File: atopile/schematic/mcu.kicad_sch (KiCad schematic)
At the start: 32 parts, among them J1 Tag-Connect_TC2030-IDC-NL_2x0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, SW1 SKRPACE010, SW2 SKRPACE010, U4 ABM8-272-T3, U5 RP2354A

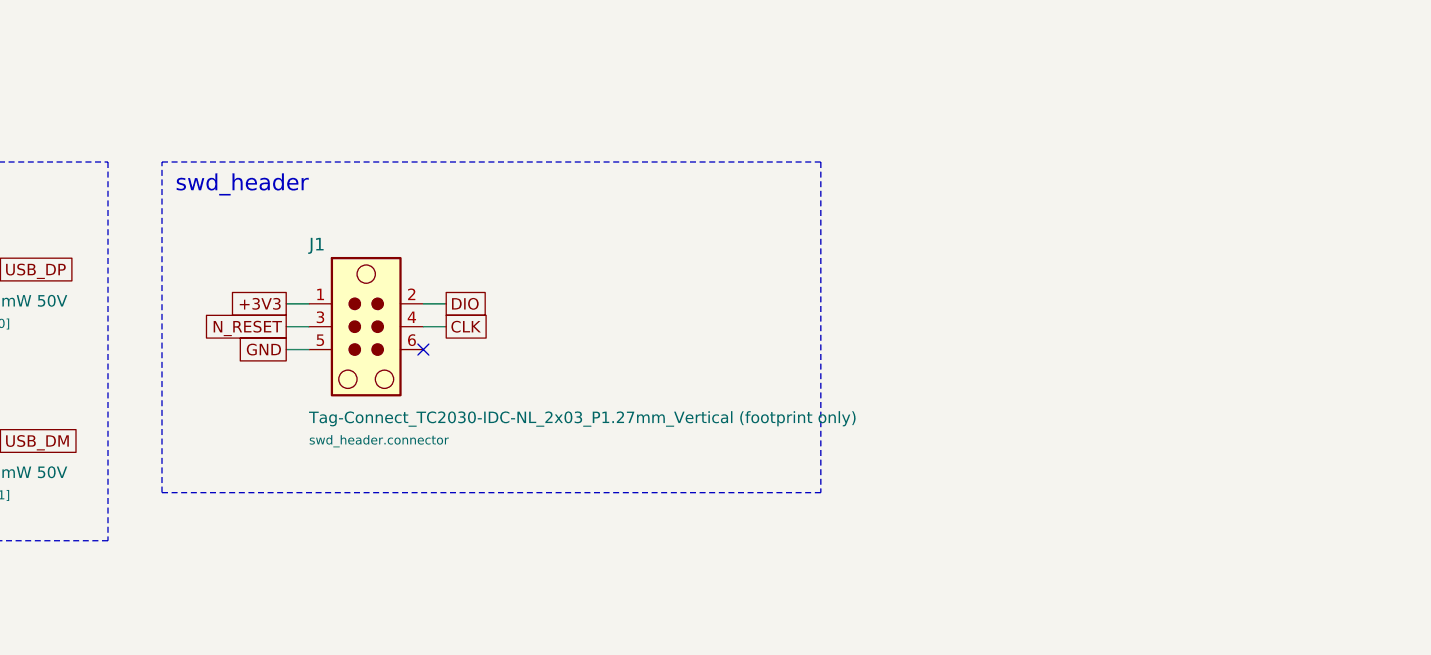
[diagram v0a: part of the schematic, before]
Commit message: Run ERC on the schematic; confirm Hi-Z command inputs are inactive
Schematic export:
- Assign real electrical pin types (datasheet-based for the ICs,
  passive otherwise); atopile's EasyEDA symbols type every pin
  input/unspecified, which gave 460 meaningless ERC violations
- Add PWR_FLAGs on the four rails fed through passives (GND, +5V,
  +1V1, VREG_AVDD), write sym/fp library tables and a project file
- Run KiCad ERC as part of the export: 0 errors, 0 warnings
  (negative test: dropping the +5V flag is reported as an error)

Manual section 9, diag 9.2 (70754 board 2): every command input has a
4.7k pull-up to +5V into TTL, contact SAMPLE a 2.2k pull-up, and pulse
SAMPLE is AC-coupled. Hi-Z outputs therefore read as inactive, and the
5.25V HCT high is within TTL ratings. Document this, plus the need to
load PULSE SAMPLE = 0 before enabling the outputs.

Co-Authored-By: Claude Opus 5.5 <noreply@anthropic.com>
Claude-Session: https://claude.ai/code/session_01NqBEt2iCuw3VMJkgzgPtpr
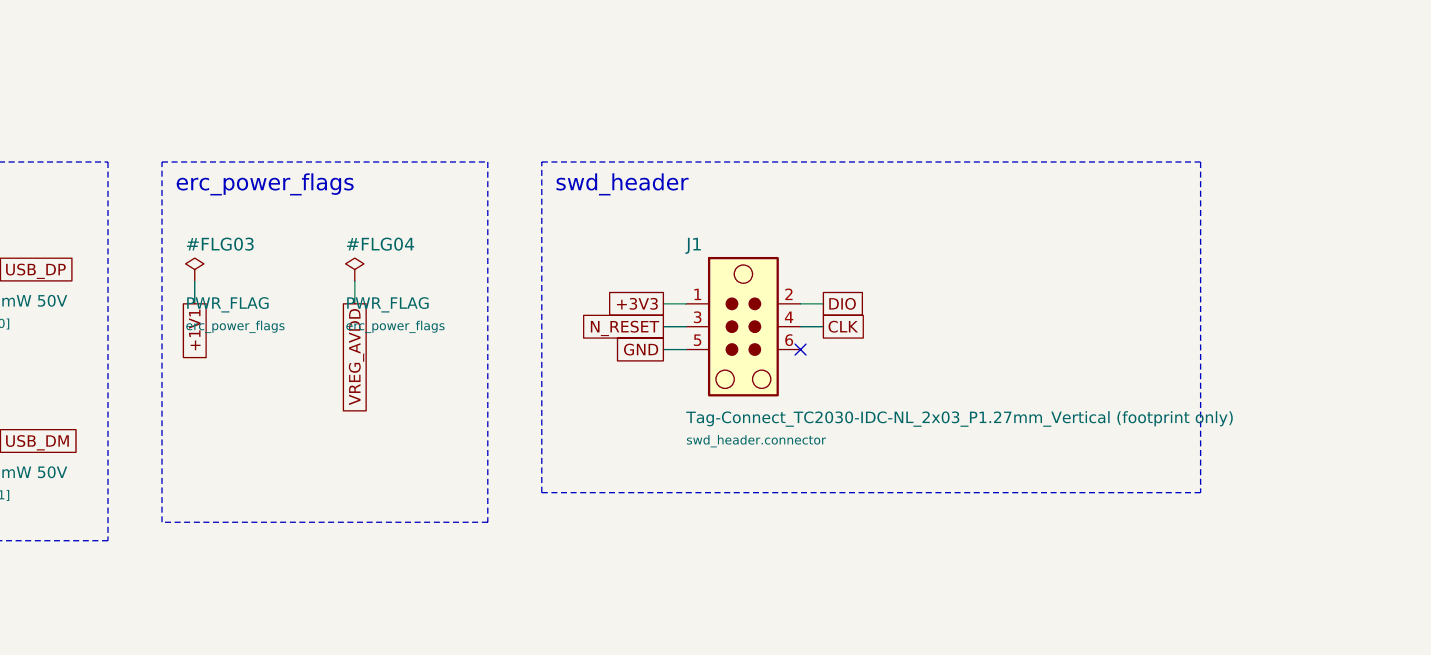
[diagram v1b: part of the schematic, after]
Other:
- note added: "erc_power_flags"
- moved on the sheet: J1
